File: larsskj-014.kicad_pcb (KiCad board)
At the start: 2 copper layers, 58 x 58 mm, 8 parts, among them J1 Conn_01x01_Pin, J2 Conn_01x01_Pin, J3 Conn_01x01_Pin, J4 Conn_01x01_Pin, J5 Conn_01x01_Pin, J6 Conn_01x01_Pin

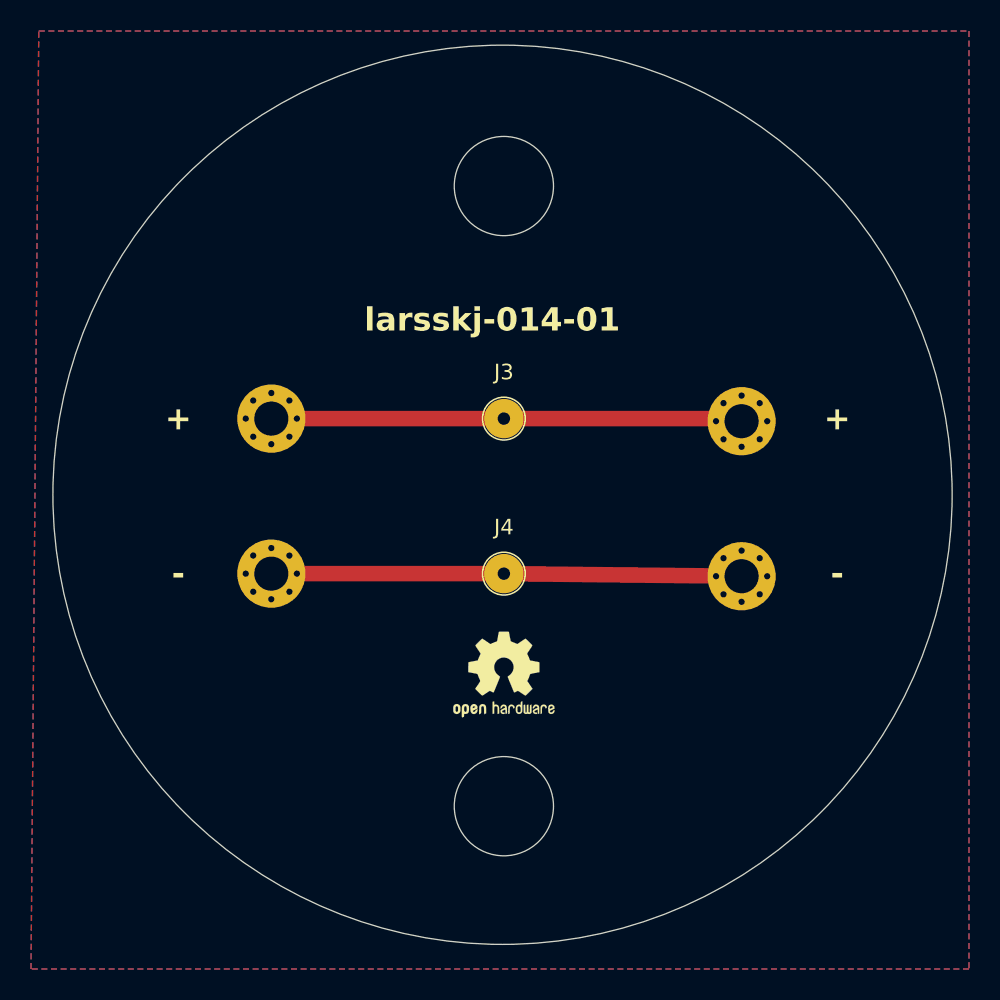
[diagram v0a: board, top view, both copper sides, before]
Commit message: Adjust to correct size.
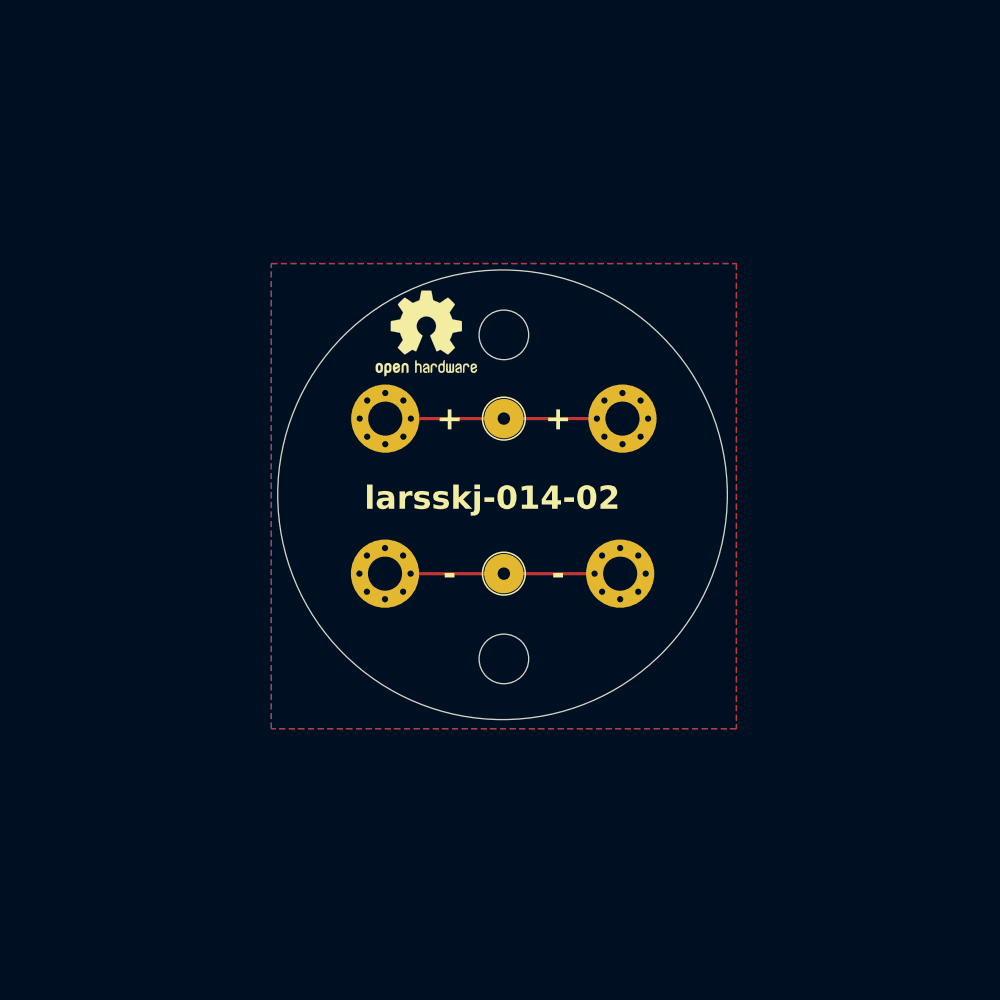
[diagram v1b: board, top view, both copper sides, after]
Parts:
- moved REF** 22.6 mm to (145.0, 89.5)
- moved REF** 22.6 mm to (155.0, 89.5)
- moved J6 7.84 mm to (157.5, 105.0)
- moved J5 7.69 mm to (157.7, 95.0)
- moved J1 7.35 mm to (142.3, 95.0)
- moved J2 7.33 mm to (142.3, 105.0)
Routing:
- net -VDC: track 0.00 -> 15.2 mm
- net +VDC: track 0.00 -> 13.7 mm
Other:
- board size 58 x 58 mm -> 29 x 29 mm
- board text added: "larsskj-014-02"
- board text removed: "larsskj-014-01"
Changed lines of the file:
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@@
 	(footprint "MountingHole:MountingHole_2.2mm_M2_Pad_Via"
 		(layer "F.Cu")
-		(at 165.333274 95.166726)
+		(at 157.65 95)
 		(descr "Mounting Hole 2.2mm, M2, generated by kicad-footprint-generator mountinghole.py")
 		(tags "mountinghole M2")
@@
 	(footprint "MountingHole:MountingHole_2.2mm_M2_Pad_Via"
 		(layer "F.Cu")
-		(at 135 95)
+		(at 142.35 95)
 		(descr "Mounting Hole 2.2mm, M2, generated by kicad-footprint-generator mountinghole.py")
 		(tags "mountinghole M2")
@@
 			(unlocked yes)
 			(layer "F.SilkS")
+			(hide yes)
 			(effects
 				(font
@@
 	(footprint "MountingHole:MountingHole_2.2mm_M2_Pad_Via"
 		(layer "F.Cu")
-		(at 165.333274 105.166726)
+		(at 157.5 105)
 		(descr "Mounting Hole 2.2mm, M2, generated by kicad-footprint-generator mountinghole.py")
 		(tags "mountinghole M2")
@@
 	(footprint "MountingHole:MountingHole_2.2mm_M2_Pad_Via"
 		(layer "F.Cu")
-		(at 135 105)
+		(at 142.333274 105)
 		(descr "Mounting Hole 2.2mm, M2, generated by kicad-footprint-generator mountinghole.py")
 		(tags "mountinghole M2")
@@
 			(unlocked yes)
 			(layer "F.SilkS")
+			(hide yes)
 			(effects
 				(font
@@
 	(footprint "Symbol:OSHW-Logo2_7.3x6mm_SilkScreen"
 		(layer "F.Cu")
-		(at 150 111.5)
+		(at 145 89.5)
 		(descr "Open Source Hardware Symbol")
 		(tags "Logo Symbol OSHW")
@@
 	(footprint "Symbol:OSHW-Logo2_7.3x6mm_SilkScreen"
 		(layer "B.Cu")
-		(at 150 111.5 180)
+		(at 155 89.5 180)
 		(descr "Open Source Hardware Symbol")
 		(tags "Logo Symbol OSHW")
@@
 		(embedded_fonts no)
 	)
-	(gr_line
-		(start 150 95)
-		(end 165.333274 95)
-		(stroke
-			(width 1)
-			(type solid)
-		)
-		(layer "F.Cu")
-		(net 1)
-	)
-	(gr_line
-		(start 150 105)
-		(end 165.333274 105.166726)
-		(stroke
-			(width 1)
-			(type solid)
-		)
-		(layer "F.Cu")
-		(net 2)
-	)
-	(gr_line
-		(start 135 105)
-		(end 150 105)
-		(stroke
-			(width 1)
-			(type solid)
-		)
-		(layer "F.Cu")
-		(net 2)
-	)
-	(gr_line
-		(start 135 95)
-		(end 150 95)
-		(stroke
-			(width 1)
-			(type solid)
-		)
-		(layer "F.Cu")
-		(net 1)
-	)
 	(gr_circle
-		(center 150 120)
-		(end 153.2 120)
+		(center 150 110.5)
+		(end 151.6 110.5)
 		(stroke
 			(width 0.05)
@@
 	)
 	(gr_circle
-		(center 150 80)
-		(end 153.2 80)
+		(center 150 89.6)
+		(end 151.6 89.6)
 		(stroke
 			(width 0.05)
@@
 	(gr_circle
 		(center 149.913217 99.913217)
-		(end 178.913217 99.913217)
+		(end 164.413217 99.913217)
 		(stroke
 			(width 0.05)
@@
 	)
 	(gr_text "+"
-		(at 171.5 95 0)
+		(at 153.5 95 0)
 		(layer "F.SilkS")
 		(effects
@@
 	)
 	(gr_text "-"
-		(at 129 105 0)
+		(at 146.5 105 0)
 		(layer "F.SilkS")
 		(effects
@@
 	)
 	(gr_text "+"
-		(at 129 95 0)
+		(at 146.5 95 0)
 		(layer "F.SilkS")
 		(effects
@@
 	)
 	(gr_text "-"
-		(at 171.5 105 0)
+		(at 153.5 105 0)
 		(layer "F.SilkS")
 		(effects
@@
 		)
 	)
-	(gr_text "larsskj-014-01"
-		(at 141 89.5 0)
+	(gr_text "larsskj-014-02"
+		(at 141 101 0)
 		(layer "F.SilkS")
 		(effects
@@
 	)
 	(gr_text "+"
-		(at 129 95 -0)
+		(at 146.5 95 -0)
 		(layer "B.SilkS")
 		(effects
@@
 		)
 	)
-	(gr_text "larsskj-014-01"
-		(at 159.5 89.5 0)
+	(gr_text "larsskj-014-02"
+		(at 159.5 101 0)
 		(layer "B.SilkS")
 		(effects
@@
 	)
 	(gr_text "-"
-		(at 171.5 105 -0)
+		(at 153.5 105 -0)
 		(layer "B.SilkS")
 		(effects
@@
 	)
 	(gr_text "+"
-		(at 171.5 95 -0)
+		(at 153.5 95 -0)
 		(layer "B.SilkS")
 		(effects
@@
 	)
 	(gr_text "-"
-		(at 129 105 -0)
+		(at 146.5 105 -0)
 		(layer "B.SilkS")
 		(effects
@@
 			(justify mirror)
 		)
+	)
+	(segment
+		(start 150 95)
+		(end 157.65 95)
+		(width 0.2)
+		(layer "F.Cu")
+		(net 1)
+	)
+	(segment
+		(start 144 95)
+		(end 150 95)
+		(width 0.2)
+		(layer "F.Cu")
+		(net 1)
+	)
+	(segment
+		(start 142.333274 105)
+		(end 150 105)
+		(width 0.2)
+		(layer "F.Cu")
+		(net 2)
+	)
+	(segment
+		(start 150 105)
+		(end 157.5 105)
+		(width 0.2)
+		(layer "F.Cu")
+		(net 2)
 	)
 	(zone
@@
 		(polygon
 			(pts
-				(xy 120 70) (xy 180 70) (xy 180 130.5) (xy 119.5 130.5)
-			)
-		)
+				(xy 135 85) (xy 165 85) (xy 165 115) (xy 135 115)
+			)
+		)

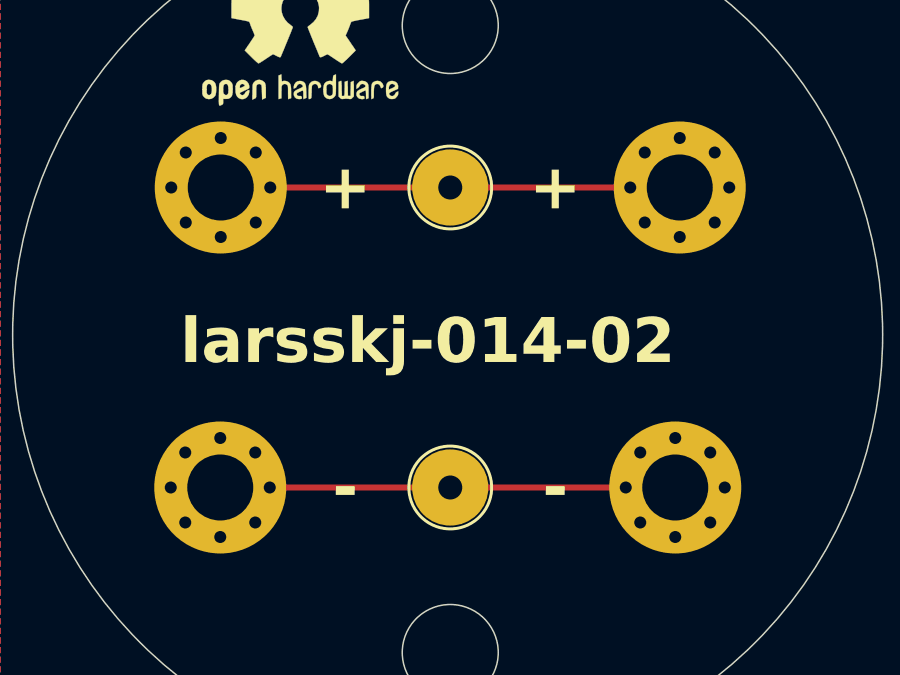
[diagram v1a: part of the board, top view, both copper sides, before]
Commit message: Widen tracks
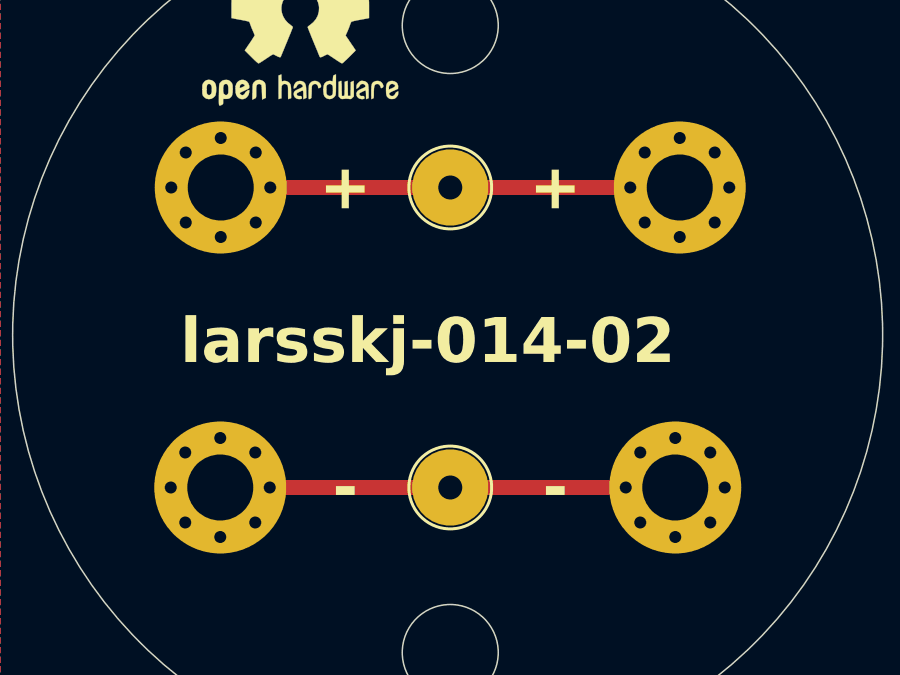
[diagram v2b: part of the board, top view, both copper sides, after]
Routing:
- net +VDC: track 13.7 -> 15.3 mm
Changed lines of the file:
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@@
 		(start 150 95)
 		(end 157.65 95)
-		(width 0.2)
+		(width 0.5)
 		(layer "F.Cu")
 		(net 1)
 	)
 	(segment
-		(start 144 95)
+		(start 142.35 95)
 		(end 150 95)
-		(width 0.2)
+		(width 0.5)
 		(layer "F.Cu")
 		(net 1)
@@
 		(start 142.333274 105)
 		(end 150 105)
-		(width 0.2)
+		(width 0.5)
 		(layer "F.Cu")
 		(net 2)
@@
 		(start 150 105)
 		(end 157.5 105)
-		(width 0.2)
+		(width 0.5)
 		(layer "F.Cu")
 		(net 2)
